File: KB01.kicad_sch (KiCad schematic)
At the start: 0 parts

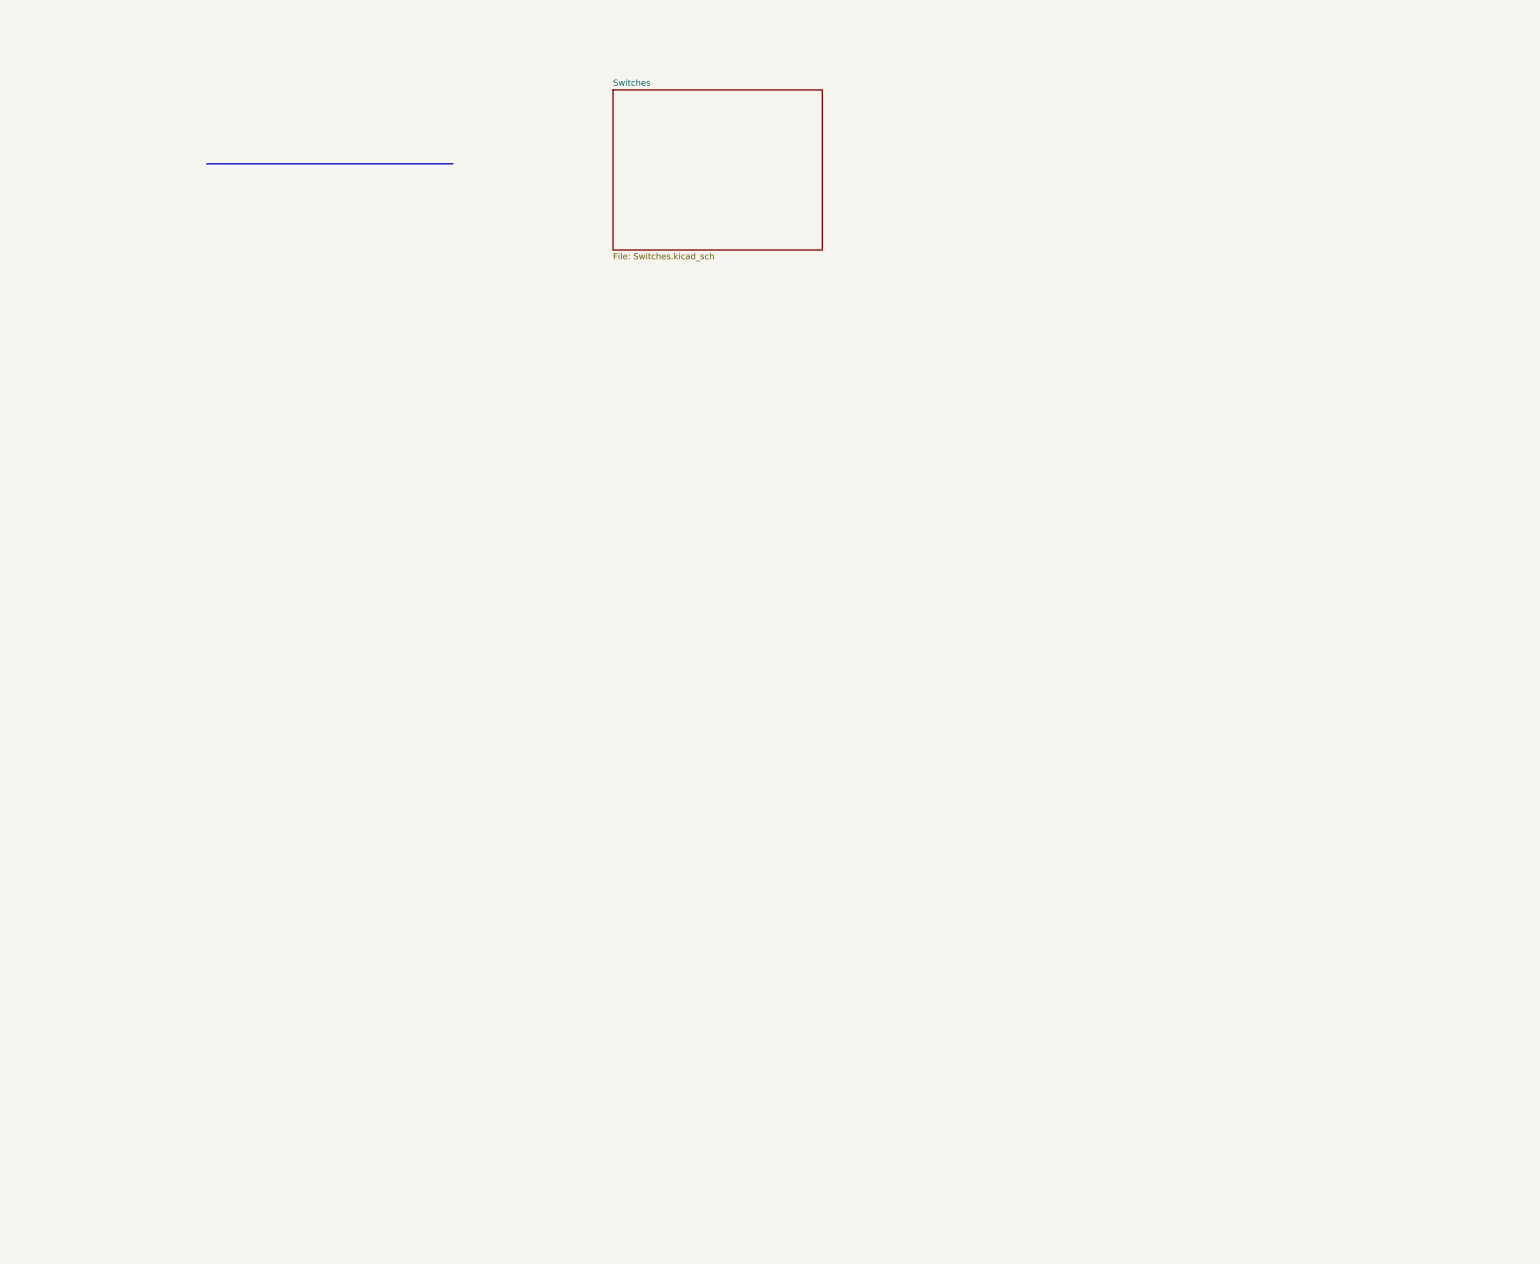
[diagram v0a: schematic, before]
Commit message: updates to board-to-board connector placement
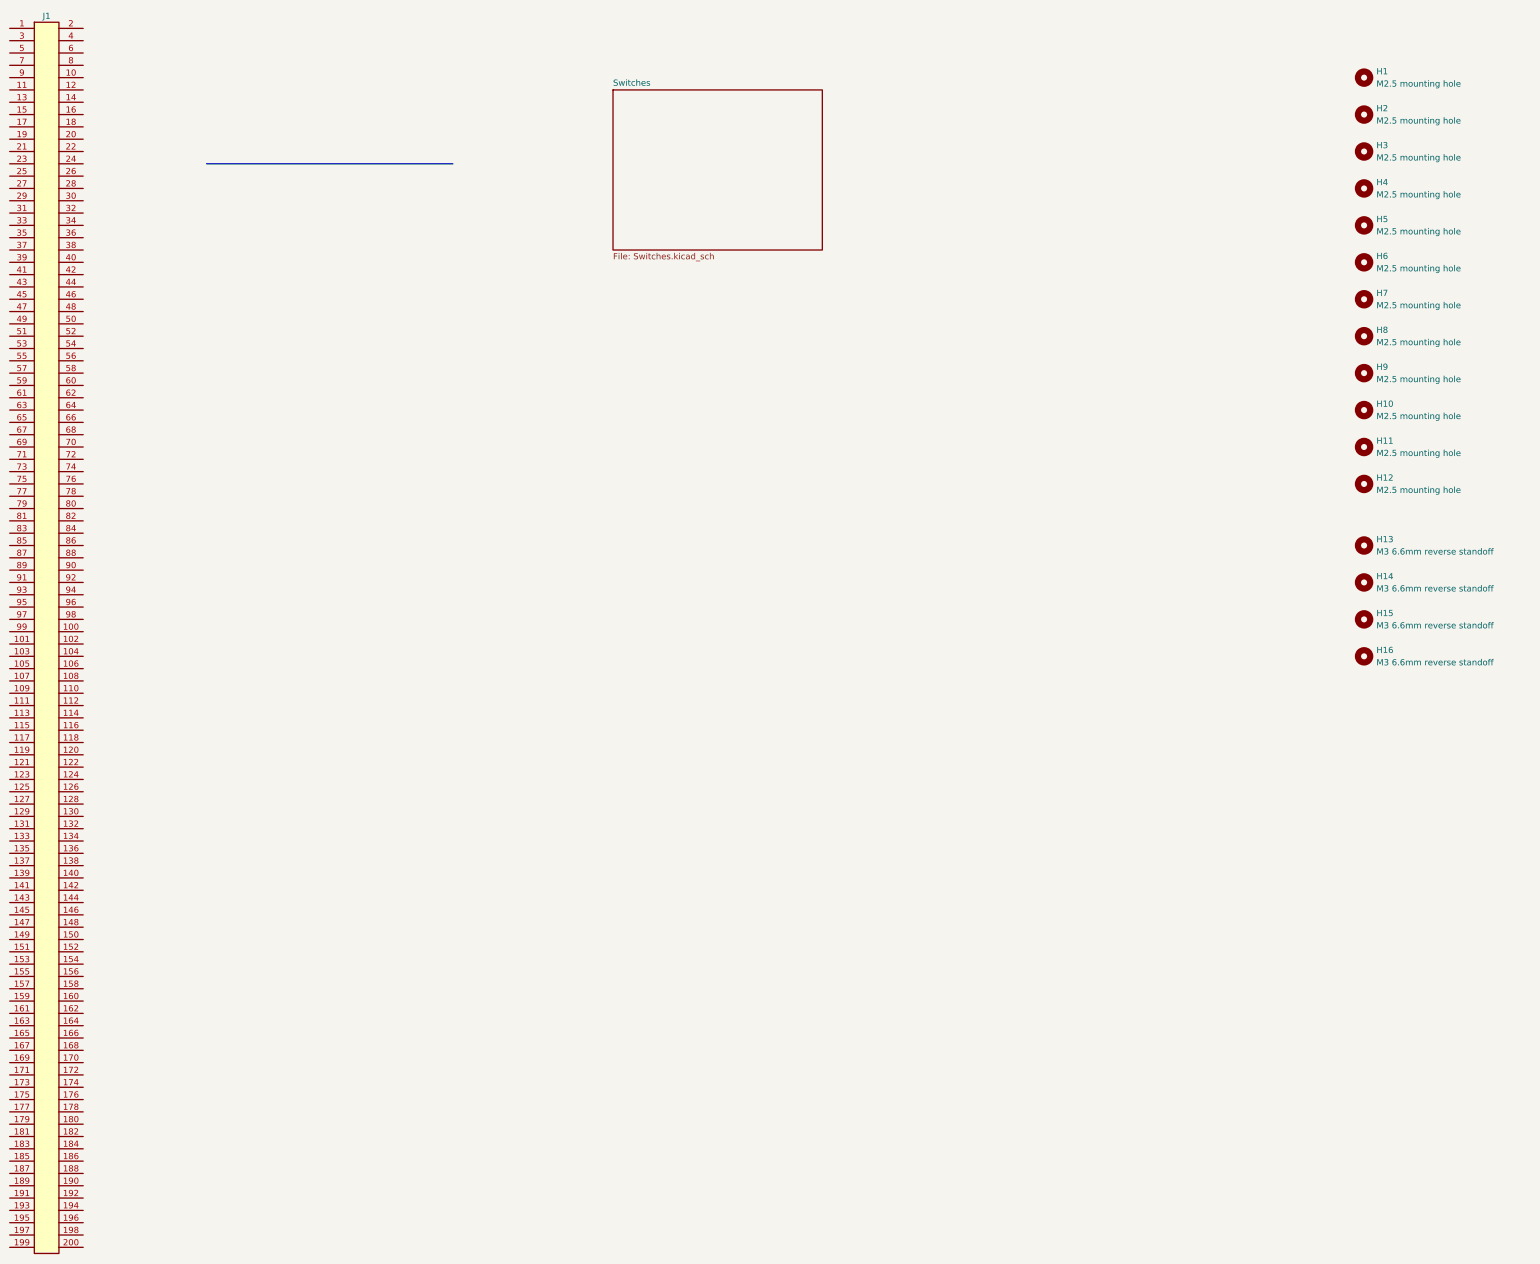
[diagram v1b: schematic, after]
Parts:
- added H1, H10, H11, H12, H2, H3, H4, H5, H6, H7, H8, H9: M2.5 mounting hole, Mech:MountingHole_2.7mm_M2.5, symbol Mech:M2.5_Mounting_Hole
- added H13, H14, H15, H16: M3 6.6mm reverse standoff, Mech:Standoff_reverse-M3-6.6mm-SMD, symbol Mech:Reverse_Standoff-6.6mm-M3-SMD
- added J1: J-Samtec_BTS-Terminal-SMD-200p, Connectors:Samtec_BTS-100-01-F-D-A, symbol Connectors:J-Samtec_BTS-Terminal-SMD-200p
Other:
- company: (none) -> Egill Milan Gunnarsson
- title: (none) -> KB01
